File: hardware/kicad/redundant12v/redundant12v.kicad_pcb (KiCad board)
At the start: 2 copper layers, 3 parts, among them U1 ATtiny212-SS, U2 MAX232CPE, X1 CXO_DIP8

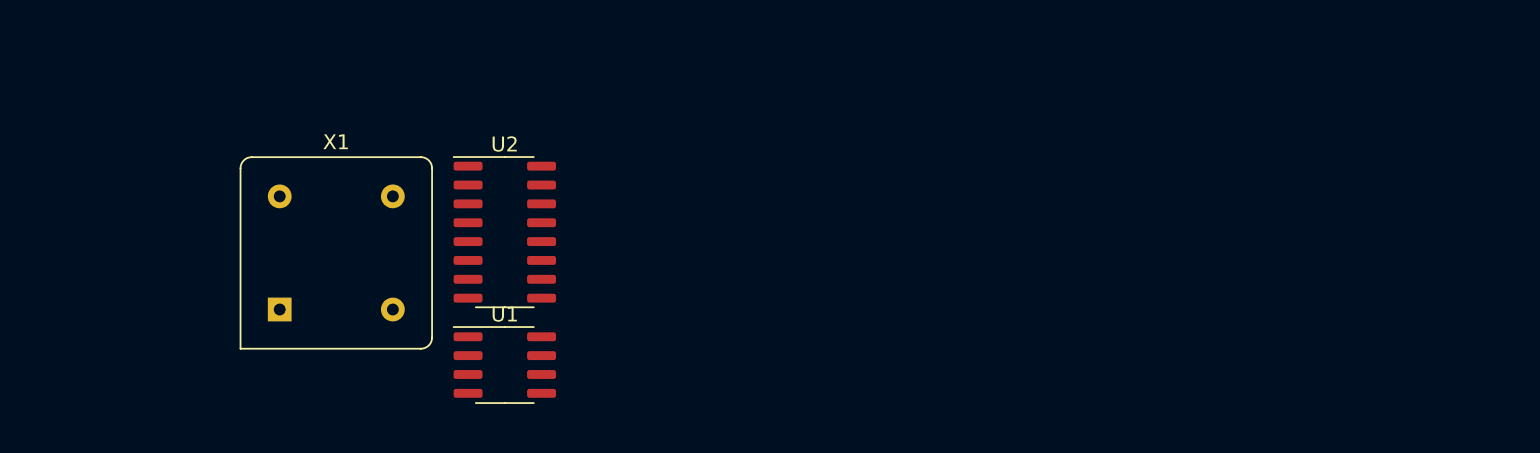
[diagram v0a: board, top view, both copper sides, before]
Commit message: Add regulator circuit and LED drivers
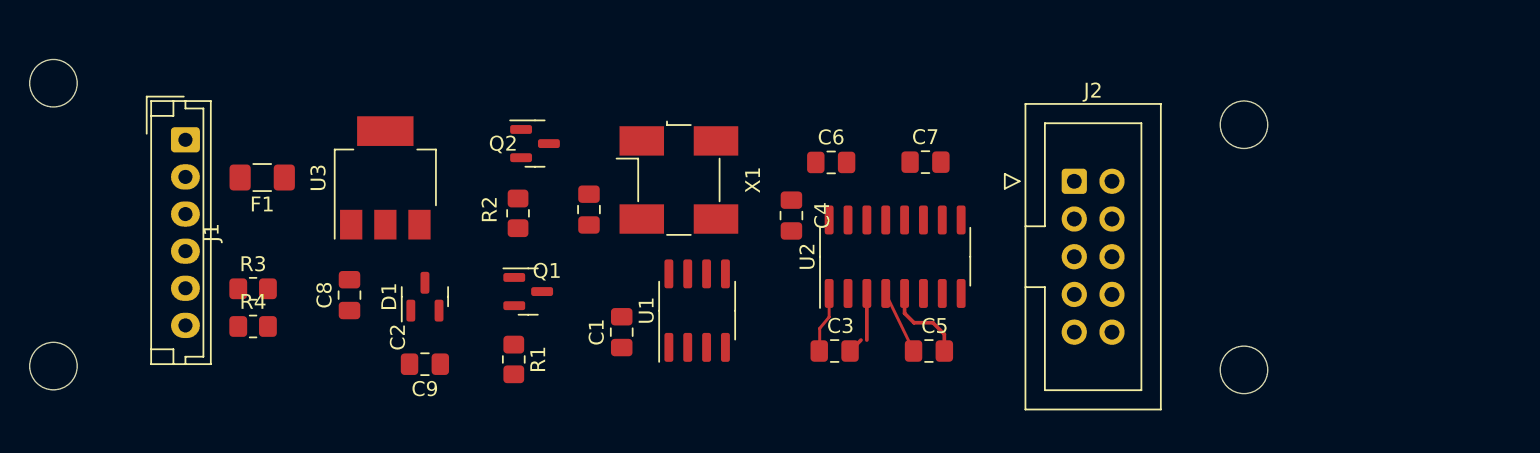
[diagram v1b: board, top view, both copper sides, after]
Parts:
- added C1: C_Small, Capacitor_SMD:C_0805_2012Metric_Pad1.18x1.45mm_HandSolder, F.Cu at (142.4, 100.6)
- added C2: C_Small, Capacitor_SMD:C_0805_2012Metric_Pad1.18x1.45mm_HandSolder, F.Cu at (140.2, 92.3)
- added C3: C_Small, Capacitor_SMD:C_0805_2012Metric_Pad1.18x1.45mm_HandSolder, F.Cu at (156.8, 101.9)
- added C4: C_Small, Capacitor_SMD:C_0805_2012Metric_Pad1.18x1.45mm_HandSolder, F.Cu at (153.8, 92.7)
- added C5: C_Small, Capacitor_SMD:C_0805_2012Metric_Pad1.18x1.45mm_HandSolder, F.Cu at (163.1, 101.9)
- added C6: C_Small, Capacitor_SMD:C_0805_2012Metric_Pad1.18x1.45mm_HandSolder, F.Cu at (156.5, 89.2)
- added C7: C_Small, Capacitor_SMD:C_0805_2012Metric_Pad1.18x1.45mm_HandSolder, F.Cu at (162.9, 89.1)
- added C8: C_Small, Capacitor_SMD:C_0805_2012Metric_Pad1.18x1.45mm_HandSolder, F.Cu at (124.1, 98.1)
- added C9: C_Small, Capacitor_SMD:C_0805_2012Metric_Pad1.18x1.45mm_HandSolder, F.Cu at (129.2, 102.7)
- added D1: BZX84Cxx, Package_TO_SOT_SMD:SOT-23, F.Cu at (129.2, 98.2)
- added F1: Fuse, Fuse:Fuse_1206_3216Metric_Pad1.42x1.75mm_HandSolder, F.Cu at (118.2, 90.2)
- added J1: Conn_01x06, Connector_JST:JST_EH_B6B-EH-A_1x06_P2.50mm_Vertical, F.Cu at (113.0, 87.6)
- added J2: Conn_02x05_Odd_Even, Connector_IDC:IDC-Header_2x05_P2.54mm_Vertical, F.Cu at (172.9, 90.4)
- added Q1: 2N3904, Package_TO_SOT_SMD:SOT-23, F.Cu at (136.1, 97.9)
- added Q2: 2N3904, Package_TO_SOT_SMD:SOT-23, F.Cu at (136.6, 87.9)
- added R1: 10K, Resistor_SMD:R_0805_2012Metric_Pad1.20x1.40mm_HandSolder, F.Cu at (135.1, 102.4)
- added R2: 10K, Resistor_SMD:R_0805_2012Metric_Pad1.20x1.40mm_HandSolder, F.Cu at (135.4, 92.6)
- added R3: R_US, Resistor_SMD:R_0805_2012Metric_Pad1.20x1.40mm_HandSolder, F.Cu at (117.6, 97.7)
- added R4: R_US, Resistor_SMD:R_0805_2012Metric_Pad1.20x1.40mm_HandSolder, F.Cu at (117.6, 100.2)
- added REF**: MountingHole_3.2mm_M3, MountingHole:MountingHole_3.2mm_M3, F.Cu at (104.1, 102.9)
- added REF**: MountingHole_3.2mm_M3, MountingHole:MountingHole_3.2mm_M3, F.Cu at (184.3, 86.6)
- added REF**: MountingHole_3.2mm_M3, MountingHole:MountingHole_3.2mm_M3, F.Cu at (104.1, 83.8)
- added REF**: MountingHole_3.2mm_M3, MountingHole:MountingHole_3.2mm_M3, F.Cu at (184.3, 103.1)
- added U3: LD1117S50TR_SOT223, Package_TO_SOT_SMD:SOT-223-3_TabPin2, F.Cu at (126.5, 90.2)
- X1: value CXO_DIP8 -> ASCO; footprint Oscillator:Oscillator_DIP-8 -> Oscillator:Oscillator_SMD_Abracon_ASV-4Pin_7.0x5.1mm_HandSoldering
- moved X1 28.3 mm to (146.3, 90.3), turned to -90 degrees
- moved U2 26.3 mm to (160.8, 95.5), turned to 90 degrees
- moved U1 13.5 mm to (147.5, 99.1), turned to 90 degrees
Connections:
- net /RX renamed RX
- net /TX renamed TX
- U1 pad 4: unconnected-(U1-Pad4) -> PS0
- U1 pad 5: unconnected-(U1-Pad5) -> PS1
- U1 pad 6: unconnected-(U1-Pad6) -> UPDI
- U1 pad 7: /EXTCLK -> EXTCLK
- X1 pad 4: GND -> VCC
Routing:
- net Net-(C5-Pad2): track 0.00 -> 5.73 mm
- net Net-(C3-Pad2): track 0.00 -> 4.18 mm

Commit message: Reorganize schematic, fix LED polarity
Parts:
- R3, R4: value R_US -> 100
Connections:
- net Net-(J1-Pad2) renamed 12V
- C8 pad 1: Net-(U3-Pad1) -> GND
- C9 pad 2: Net-(U3-Pad1) -> GND
- D1 pad 1: Net-(U3-Pad1) -> GND
- J1 pad 5: Net-(R3-Pad1) -> LED0+
- J1 pad 6: Net-(R4-Pad1) -> LED1+
- Q1 pad 1: GND -> Net-(Q1-Pad1)
- Q1 pad 3: Net-(R3-Pad2) -> VCC
- Q2 pad 1: GND -> Net-(Q2-Pad1)
- Q2 pad 3: Net-(R4-Pad2) -> VCC
- R1 pad 1: PS0 -> VCC
- R1 pad 2: VCC -> PS0
- R2 pad 1: PS1 -> VCC
- R2 pad 2: VCC -> PS1
- R3 pad 1: Net-(R3-Pad1) -> Net-(Q1-Pad1)
- R3 pad 2: Net-(R3-Pad2) -> LED0+
- R4 pad 1: Net-(R4-Pad1) -> Net-(Q2-Pad1)
- R4 pad 2: Net-(R4-Pad2) -> LED1+
- U3 pad 1: Net-(U3-Pad1) -> GND
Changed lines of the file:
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@@
   (net 30 "unconnected-(J2-Pad9)")
   (net 31 "unconnected-(J2-Pad10)")
-  (net 32 "Net-(R3-Pad2)")
-  (net 33 "Net-(R4-Pad2)")
-  (net 34 "Net-(R3-Pad1)")
-  (net 35 "Net-(R4-Pad1)")
+  (net 32 "Net-(C8-Pad2)")
+  (net 33 "12V")
+  (net 34 "LED0+")
+  (net 35 "LED1+")
   (net 36 "unconnected-(D1-Pad2)")
-  (net 37 "Net-(U3-Pad1)")
-  (net 38 "Net-(U3-Pad3)")
-  (net 39 "Net-(J1-Pad2)")
+  (net 37 "Net-(Q1-Pad1)")
+  (net 38 "Net-(Q2-Pad1)")
   (footprint "Capacitor_SMD:C_0805_2012Metric_Pad1.18x1.45mm_HandSolder" (layer "F.Cu")
     (at 124.079 98.0905 90)
@@
     (fp_line (start 1 0.625) (end -1 0.625) (layer "F.Fab") (width 0.1))
     (pad "1" smd roundrect (at -1.0375 0 90) (size 1.175 1.45) (layers "F.Cu" "F.Paste" "F.Mask") (roundrect_rratio 0.212766)
-      (net 37 "Net-(U3-Pad1)") (pintype "passive"))
+      (net 5 "GND") (pintype "passive"))
     (pad "2" smd roundrect (at 1.0375 0 90) (size 1.175 1.45) (layers "F.Cu" "F.Paste" "F.Mask") (roundrect_rratio 0.212766)
-      (net 38 "Net-(U3-Pad3)") (pintype "passive"))
+      (net 32 "Net-(C8-Pad2)") (pintype "passive"))
     (model "${KICAD6_3DMODEL_DIR}/Capacitor_SMD.3dshapes/C_0805_2012Metric.wrl"
       (offset (xyz 0 0 0))
@@
       (effects (font (size 1 1) (thickness 0.15)))
     )
-    (fp_text value "R_US" (at 0 1.65) (layer "F.Fab")
+    (fp_text value "100" (at 0 1.65) (layer "F.Fab")
       (effects (font (size 1 1) (thickness 0.15)))
     )
@@
     (fp_line (start 1 0.625) (end -1 0.625) (layer "F.Fab") (width 0.1))
     (pad "1" smd roundrect (at -1 0) (size 1.2 1.4) (layers "F.Cu" "F.Paste" "F.Mask") (roundrect_rratio 0.208333)
-      (net 34 "Net-(R3-Pad1)") (pintype "passive"))
+      (net 37 "Net-(Q1-Pad1)") (pintype "passive"))
     (pad "2" smd roundrect (at 1 0) (size 1.2 1.4) (layers "F.Cu" "F.Paste" "F.Mask") (roundrect_rratio 0.208333)
-      (net 32 "Net-(R3-Pad2)") (pintype "passive"))
+      (net 34 "LED0+") (pintype "passive"))
     (model "${KICAD6_3DMODEL_DIR}/Resistor_SMD.3dshapes/R_0805_2012Metric.wrl"
       (offset (xyz 0 0 0))
@@
       (net 1 "VCC") (pintype "passive"))
     (pad "2" smd roundrect (at 1.0375 0 180) (size 1.175 1.45) (layers "F.Cu" "F.Paste" "F.Mask") (roundrect_rratio 0.212766)
-      (net 37 "Net-(U3-Pad1)") (pintype "passive"))
+      (net 5 "GND") (pintype "passive"))
     (model "${KICAD6_3DMODEL_DIR}/Capacitor_SMD.3dshapes/C_0805_2012Metric.wrl"
       (offset (xyz 0 0 0))
@@
       (net 5 "GND") (pinfunction "Pin_1") (pintype "passive"))
     (pad "2" thru_hole oval (at 2.5 0 270) (size 1.7 1.95) (drill 0.95) (layers *.Cu *.Mask)
-      (net 39 "Net-(J1-Pad2)") (pinfunction "Pin_2") (pintype "passive"))
+      (net 33 "12V") (pinfunction "Pin_2") (pintype "passive"))
     (pad "3" thru_hole oval (at 5 0 270) (size 1.7 1.95) (drill 0.95) (layers *.Cu *.Mask)
       (net 19 "PS0") (pinfunction "Pin_3") (pintype "passive"))
@@
       (net 20 "PS1") (pinfunction "Pin_4") (pintype "passive"))
     (pad "5" thru_hole oval (at 10 0 270) (size 1.7 1.95) (drill 0.95) (layers *.Cu *.Mask)
-      (net 34 "Net-(R3-Pad1)") (pinfunction "Pin_5") (pintype "passive"))
+      (net 34 "LED0+") (pinfunction "Pin_5") (pintype "passive"))
     (pad "6" thru_hole oval (at 12.5 0 270) (size 1.7 1.95) (drill 0.95) (layers *.Cu *.Mask)
-      (net 35 "Net-(R4-Pad1)") (pinfunction "Pin_6") (pintype "passive"))
+      (net 35 "LED1+") (pinfunction "Pin_6") (pintype "passive"))
     (model "${KICAD6_3DMODEL_DIR}/Connector_JST.3dshapes/JST_EH_B6B-EH-A_1x06_P2.50mm_Vertical.wrl"
       (offset (xyz 0 0 0))
@@
     (fp_line (start 1.6 -0.8) (end 1.6 0.8) (layer "F.Fab") (width 0.1))
     (pad "1" smd roundrect (at -1.4875 0 180) (size 1.425 1.75) (layers "F.Cu" "F.Paste" "F.Mask") (roundrect_rratio 0.175439)
-      (net 38 "Net-(U3-Pad3)") (pintype "passive"))
+      (net 32 "Net-(C8-Pad2)") (pintype "passive"))
     (pad "2" smd roundrect (at 1.4875 0 180) (size 1.425 1.75) (layers "F.Cu" "F.Paste" "F.Mask") (roundrect_rratio 0.175439)
-      (net 39 "Net-(J1-Pad2)") (pintype "passive"))
+      (net 33 "12V") (pintype "passive"))
     (model "${KICAD6_3DMODEL_DIR}/Fuse.3dshapes/Fuse_1206_3216Metric.wrl"
       (offset (xyz 0 0 0))
@@
     (fp_line (start 0.65 1.45) (end -0.65 1.45) (layer "F.Fab") (width 0.1))
     (pad "1" smd roundrect (at -0.9375 -0.95) (size 1.475 0.6) (layers "F.Cu" "F.Paste" "F.Mask") (roundrect_rratio 0.25)
-      (net 5 "GND") (pinfunction "E") (pintype "passive"))
+      (net 38 "Net-(Q2-Pad1)") (pinfunction "E") (pintype "passive"))
     (pad "2" smd roundrect (at -0.9375 0.95) (size 1.475 0.6) (layers "F.Cu" "F.Paste" "F.Mask") (roundrect_rratio 0.25)
       (net 20 "PS1") (pinfunction "B") (pintype "passive"))
     (pad "3" smd roundrect (at 0.9375 0) (size 1.475 0.6) (layers "F.Cu" "F.Paste" "F.Mask") (roundrect_rratio 0.25)
-      (net 33 "Net-(R4-Pad2)") (pinfunction "C") (pintype "passive"))
+      (net 1 "VCC") (pinfunction "C") (pintype "passive"))
     (model "${KICAD6_3DMODEL_DIR}/Package_TO_SOT_SMD.3dshapes/SOT-23.wrl"
       (offset (xyz 0 0 0))
@@
       (effects (font (size 1 1) (thickness 0.15)))
     )
-    (fp_text value "R_US" (at 0 1.65) (layer "F.Fab")
+    (fp_text value "100" (at 0 1.65) (layer "F.Fab")
       (effects (font (size 1 1) (thickness 0.15)))
     )
@@
     (fp_line (start 1 -0.625) (end 1 0.625) (layer "F.Fab") (width 0.1))
     (pad "1" smd roundrect (at -1 0) (size 1.2 1.4) (layers "F.Cu" "F.Paste" "F.Mask") (roundrect_rratio 0.208333)
-      (net 35 "Net-(R4-Pad1)") (pintype "passive"))
+      (net 38 "Net-(Q2-Pad1)") (pintype "passive"))
     (pad "2" smd roundrect (at 1 0) (size 1.2 1.4) (layers "F.Cu" "F.Paste" "F.Mask") (roundrect_rratio 0.208333)
-      (net 33 "Net-(R4-Pad2)") (pintype "passive"))
+      (net 35 "LED1+") (pintype "passive"))
     (model "${KICAD6_3DMODEL_DIR}/Resistor_SMD.3dshapes/R_0805_2012Metric.wrl"
       (offset (xyz 0 0 0))
@@
     (fp_line (start -1.85 3.35) (end 1.85 3.35) (layer "F.Fab") (width 0.1))
     (pad "1" smd rect (at -3.15 -2.3 90) (size 2 1.5) (layers "F.Cu" "F.Paste" "F.Mask")
-      (net 37 "Net-(U3-Pad1)") (pinfunction "GND") (pintype "power_in"))
+      (net 5 "GND") (pinfunction "GND") (pintype "power_in"))
     (pad "2" smd rect (at -3.15 0 90) (size 2 1.5) (layers "F.Cu" "F.Paste" "F.Mask")
       (net 1 "VCC") (pinfunction "VO") (pintype "power_out"))
@@
       (net 1 "VCC") (pinfunction "VO") (pintype "power_out"))
     (pad "3" smd rect (at -3.15 2.3 90) (size 2 1.5) (layers "F.Cu" "F.Paste" "F.Mask")
-      (net 38 "Net-(U3-Pad3)") (pinfunction "VI") (pintype "power_in"))
+      (net 32 "Net-(C8-Pad2)") (pinfunction "VI") (pintype "power_in"))
     (model "${KICAD6_3DMODEL_DIR}/Package_TO_SOT_SMD.3dshapes/SOT-223.wrl"
       (offset (xyz 0 0 0))
@@
     (fp_line (start 0.65 1.45) (end -0.65 1.45) (layer "F.Fab") (width 0.1))
     (pad "1" smd roundrect (at -0.9375 -0.95 90) (size 1.475 0.6) (layers "F.Cu" "F.Paste" "F.Mask") (roundrect_rratio 0.25)
-      (net 37 "Net-(U3-Pad1)") (pinfunction "A") (pintype "passive"))
+      (net 5 "GND") (pinfunction "A") (pintype "passive"))
     (pad "2" smd roundrect (at -0.9375 0.95 90) (size 1.475 0.6) (layers "F.Cu" "F.Paste" "F.Mask") (roundrect_rratio 0.25)
       (net 36 "unconnected-(D1-Pad2)") (pinfunction "NC") (pintype "no_connect"))
     (pad "3" smd roundrect (at 0.9375 0 90) (size 1.475 0.6) (layers "F.Cu" "F.Paste" "F.Mask") (roundrect_rratio 0.25)
-      (net 38 "Net-(U3-Pad3)") (pinfunction "K") (pintype "passive"))
+      (net 32 "Net-(C8-Pad2)") (pinfunction "K") (pintype "passive"))
     (model "${KICAD6_3DMODEL_DIR}/Package_TO_SOT_SMD.3dshapes/SOT-23.wrl"
       (offset (xyz 0 0 0))
@@
     (fp_line (start -0.65 1.45) (end -0.65 -1.125) (layer "F.Fab") (width 0.1))
     (pad "1" smd roundrect (at -0.9375 -0.95) (size 1.475 0.6) (layers "F.Cu" "F.Paste" "F.Mask") (roundrect_rratio 0.25)
-      (net 5 "GND") (pinfunction "E") (pintype "passive"))
+      (net 37 "Net-(Q1-Pad1)") (pinfunction "E") (pintype "passive"))
     (pad "2" smd roundrect (at -0.9375 0.95) (size 1.475 0.6) (layers "F.Cu" "F.Paste" "F.Mask") (roundrect_rratio 0.25)
       (net 19 "PS0") (pinfunction "B") (pintype "passive"))
     (pad "3" smd roundrect (at 0.9375 0) (size 1.475 0.6) (layers "F.Cu" "F.Paste" "F.Mask") (roundrect_rratio 0.25)
-      (net 32 "Net-(R3-Pad2)") (pinfunction "C") (pintype "passive"))
+      (net 1 "VCC") (pinfunction "C") (pintype "passive"))
     (model "${KICAD6_3DMODEL_DIR}/Package_TO_SOT_SMD.3dshapes/SOT-23.wrl"
       (offset (xyz 0 0 0))
@@
     (fp_line (start 1 0.625) (end -1 0.625) (layer "F.Fab") (width 0.1))
     (pad "1" smd roundrect (at -1 0 90) (size 1.2 1.4) (layers "F.Cu" "F.Paste" "F.Mask") (roundrect_rratio 0.208333)
+      (net 1 "VCC") (pintype "passive"))
+    (pad "2" smd roundrect (at 1 0 90) (size 1.2 1.4) (layers "F.Cu" "F.Paste" "F.Mask") (roundrect_rratio 0.208333)
       (net 20 "PS1") (pintype "passive"))
-    (pad "2" smd roundrect (at 1 0 90) (size 1.2 1.4) (layers "F.Cu" "F.Paste" "F.Mask") (roundrect_rratio 0.208333)
-      (net 1 "VCC") (pintype "passive"))
     (model "${KICAD6_3DMODEL_DIR}/Resistor_SMD.3dshapes/R_0805_2012Metric.wrl"
       (offset (xyz 0 0 0))
@@
     (fp_line (start 1 -0.625) (end 1 0.625) (layer "F.Fab") (width 0.1))
     (pad "1" smd roundrect (at -1 0 270) (size 1.2 1.4) (layers "F.Cu" "F.Paste" "F.Mask") (roundrect_rratio 0.208333)
+      (net 1 "VCC") (pintype "passive"))
+    (pad "2" smd roundrect (at 1 0 270) (size 1.2 1.4) (layers "F.Cu" "F.Paste" "F.Mask") (roundrect_rratio 0.208333)
       (net 19 "PS0") (pintype "passive"))
-    (pad "2" smd roundrect (at 1 0 270) (size 1.2 1.4) (layers "F.Cu" "F.Paste" "F.Mask") (roundrect_rratio 0.208333)
-      (net 1 "VCC") (pintype "passive"))
     (model "${KICAD6_3DMODEL_DIR}/Resistor_SMD.3dshapes/R_0805_2012Metric.wrl"
       (offset (xyz 0 0 0))
